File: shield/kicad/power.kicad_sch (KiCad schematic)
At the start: 23 parts, among them Q1 NTR4101PT1G, Q2 DMG1012T-7, Q3 DMG1012T-7, Q4 NTR4101PT1G, Q5 DMG1012T-7, Q6 DMG1012T-7, U1 BQ25060DQCR, U2 Texas Instruments TPS3422EGDR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, U3 STC3100IST, U4 Texas Instruments TPS63060DSCR, U5 MAX803SQ293D2T1G

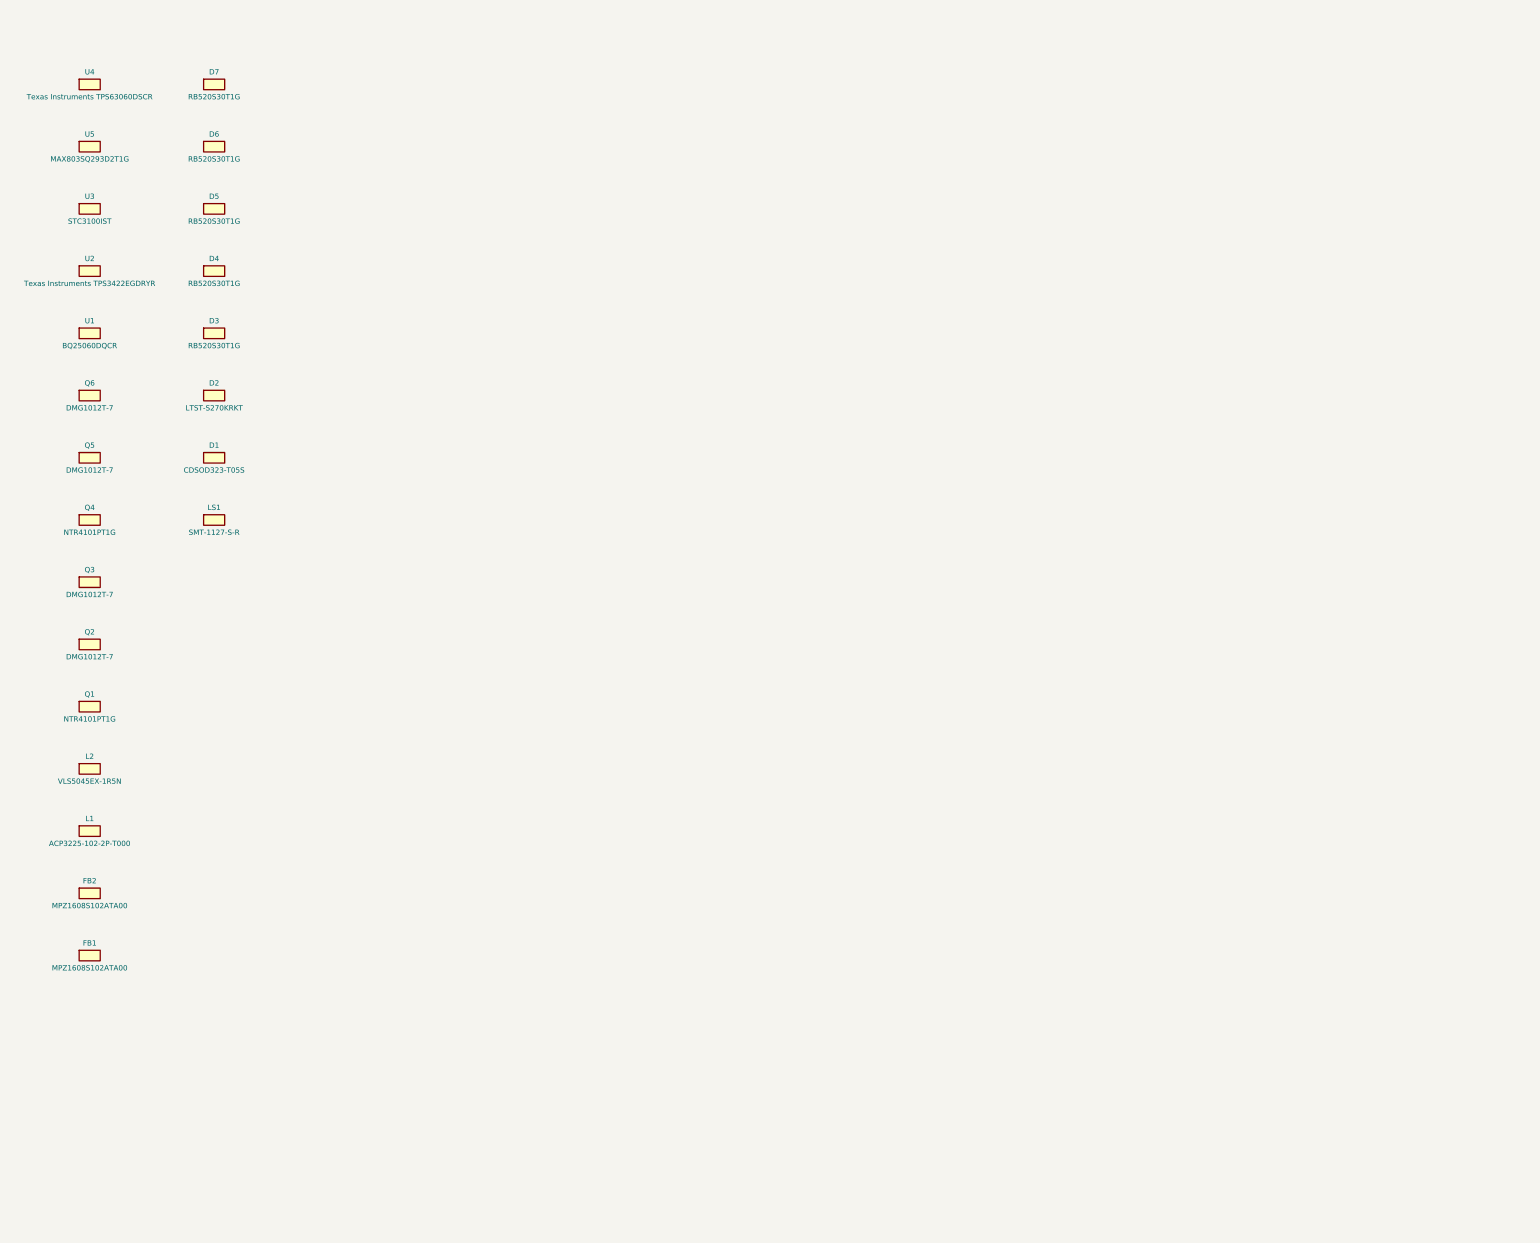
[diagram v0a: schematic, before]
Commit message: Complete schematic wiring, footprint assignments, and validation renders
- Generated proper KiCad symbols with pin definitions for all 139 components
- Created 2 hierarchical sub-sheets: Power Supply and Peripherals & Connectors
- Added schematic wiring with net labels (VBUS, VBAT, V3V3, GND, I2C, SPI, etc.)
- Assigned KiCad standard library footprints to all components
- Rendered schematic and PCB SVGs using kicad-cli-nightly
- Ran ERC and DRC validation
- Updated README with rendered images and footprint assignment table

Agent-Logs-Url: https://github.com/3rdIteration/specter-diy/sessions/67aa0d59-b533-4f87-a3fd-0109cc63ae2b

Co-authored-by: 3rdIteration <2230318+3rdIteration@users.noreply.github.com>
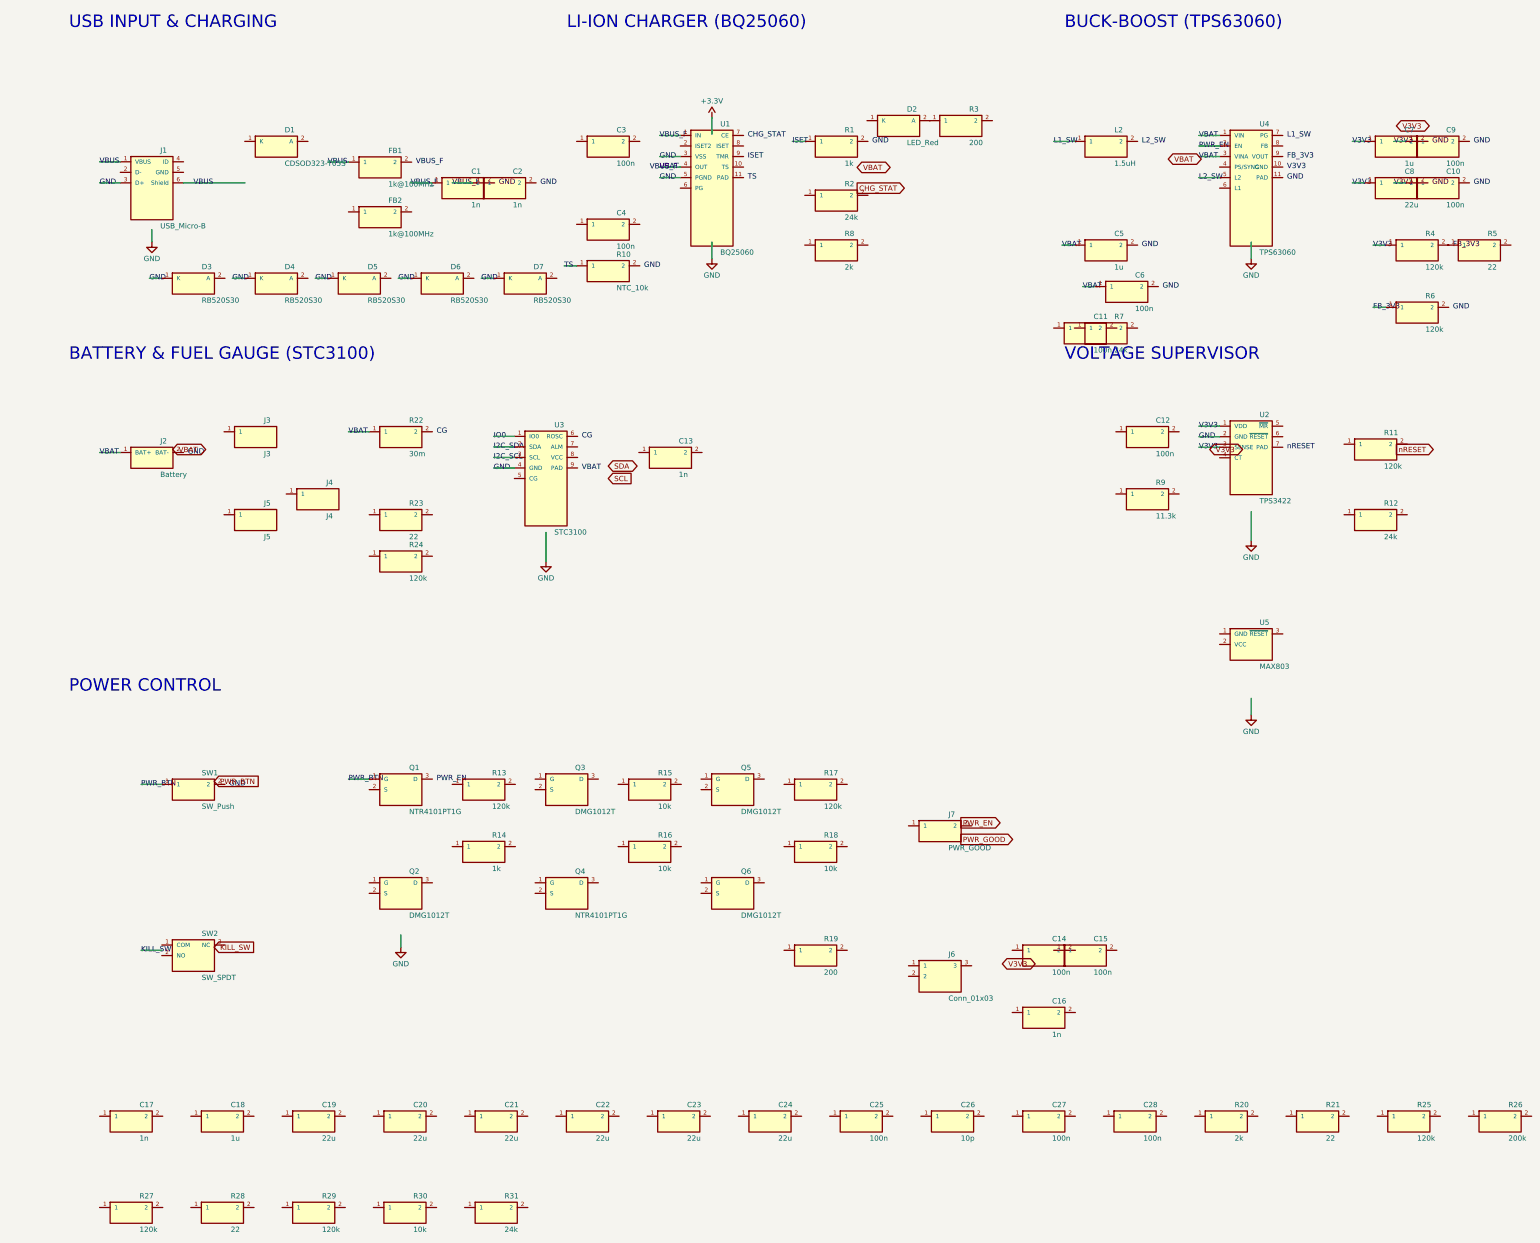
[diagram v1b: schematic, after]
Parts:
- removed D1: CDSOD323-T05S, PCB-svuptgvsz8fymjeirekr-1, symbol specter_shield:D1
- removed D2: LTST-S270KRKT, PCB_-_LS_A67K, symbol specter_shield:D2
- removed D3: RB520S30T1G, ONSC-SOD-523-2-502-01_V, symbol specter_shield:D3
- removed D4: RB520S30T1G, ONSC-SOD-523-2-502-01_V, symbol specter_shield:D4
- removed D5: RB520S30T1G, ONSC-SOD-523-2-502-01_V, symbol specter_shield:D5
- removed D6: RB520S30T1G, ONSC-SOD-523-2-502-01_V, symbol specter_shield:D6
- removed D7: RB520S30T1G, ONSC-SOD-523-2-502-01_V, symbol specter_shield:D7
- removed FB1: MPZ1608S102ATA00, PCB-lzgidm1lbgbngdte6jvy-1, symbol specter_shield:FB1
- removed FB2: MPZ1608S102ATA00, PCB-lzgidm1lbgbngdte6jvy-1, symbol specter_shield:FB2
- removed L1: ACP3225-102-2P-T000, PCB-59e4j6y0bn8hbujw2jpq-1, symbol specter_shield:L1
- removed L2: VLS5045EX-1R5N, VLS5045EX-1R5N, symbol specter_shield:L2
- removed LS1: SMT-1127-S-R, PCB-s69sc097nywe4t4ay05e-1, symbol specter_shield:LS1
- removed Q1: NTR4101PT1G, ONSC-SOT-23-3-318-08_V, symbol specter_shield:Q1
- removed Q2: DMG1012T-7, PCB-829213-1, symbol specter_shield:Q2
- removed Q3: DMG1012T-7, PCB-829213-1, symbol specter_shield:Q3
- removed Q4: NTR4101PT1G, ONSC-SOT-23-3-318-08_V, symbol specter_shield:Q4
- removed Q5: DMG1012T-7, PCB-829213-1, symbol specter_shield:Q5
- removed Q6: DMG1012T-7, PCB-829213-1, symbol specter_shield:Q6
- removed U1: BQ25060DQCR, DQC10-2400X840TP, symbol specter_shield:U1
- removed U2: Texas Instruments TPS3422EGDRYR, PCB-yhvz6iwei78a9n514jnh-1, symbol specter_shield:U2
- removed U3: STC3100IST, PCB-2tv7dotjw6i7jk8dmo5t-1, symbol specter_shield:U3
- removed U4: Texas Instruments TPS63060DSCR, TPS63060, symbol specter_shield:U4
- removed U5: MAX803SQ293D2T1G, PCB-cot7ps8saw6rws0ryicd-1, symbol specter_shield:U5
- added C1: 1n, Capacitor_SMD:C_0402_1005Metric, symbol C1
- added C10: 100n, Capacitor_SMD:C_0402_1005Metric, symbol C10
- added C11: 100n, Capacitor_SMD:C_0402_1005Metric, symbol C11
- added C12: 100n, Capacitor_SMD:C_0402_1005Metric, symbol C12
- added C13: 1n, Capacitor_SMD:C_0402_1005Metric, symbol C13
- added C14: 100n, Capacitor_SMD:C_0402_1005Metric, symbol C14
- added C15: 100n, Capacitor_SMD:C_0402_1005Metric, symbol C15
- added C16: 1n, Capacitor_SMD:C_0402_1005Metric, symbol C16
- added C17: 1n, Capacitor_SMD:C_0402_1005Metric, symbol C17
- added C18: 1u, Capacitor_SMD:C_0402_1005Metric, symbol C18
- added C19: 22u, Capacitor_SMD:C_0805_2012Metric, symbol C19
- added C2: 1n, Capacitor_SMD:C_0402_1005Metric, symbol C2
- added C20: 22u, Capacitor_SMD:C_0805_2012Metric, symbol C20
- added C21: 22u, Capacitor_SMD:C_0805_2012Metric, symbol C21
- added C22: 22u, Capacitor_SMD:C_0805_2012Metric, symbol C22
- added C23: 22u, Capacitor_SMD:C_0805_2012Metric, symbol C23
- added C24: 22u, Capacitor_SMD:C_0805_2012Metric, symbol C24
- added C25: 100n, Capacitor_SMD:C_0402_1005Metric, symbol C25
- added C26: 10p, Capacitor_SMD:C_0402_1005Metric, symbol C26
- added C27: 100n, Capacitor_SMD:C_0402_1005Metric, symbol C27
- added C28: 100n, Capacitor_SMD:C_0402_1005Metric, symbol C28
- added C3: 100n, Capacitor_SMD:C_0402_1005Metric, symbol C3
- added C4: 100n, Capacitor_SMD:C_0402_1005Metric, symbol C4
- added C5: 1u, Capacitor_SMD:C_0402_1005Metric, symbol C5
- added C6: 100n, Capacitor_SMD:C_0402_1005Metric, symbol C6
- added C7: 1u, Capacitor_SMD:C_0402_1005Metric, symbol C7
- added C8: 22u, Capacitor_SMD:C_0805_2012Metric, symbol C8
- added C9: 100n, Capacitor_SMD:C_0402_1005Metric, symbol C9
- added D1: CDSOD323-T05S, Diode_SMD:D_SOD-323, symbol D1
- added D2: LED_Red, LED_SMD:LED_0603_1608Metric, symbol D2
- added D3: RB520S30, Diode_SMD:D_SOD-523, symbol D3
- added D4: RB520S30, Diode_SMD:D_SOD-523, symbol D4
- added D5: RB520S30, Diode_SMD:D_SOD-523, symbol D5
- added D6: RB520S30, Diode_SMD:D_SOD-523, symbol D6
- added D7: RB520S30, Diode_SMD:D_SOD-523, symbol D7
- added FB1: 1k@100MHz, Inductor_SMD:L_0603_1608Metric, symbol FB1
- added FB2: 1k@100MHz, Inductor_SMD:L_0603_1608Metric, symbol FB2
- added J1: USB_Micro-B, Connector_USB:USB_Micro-B_Molex_47346-0001, symbol J1
- added J2: Battery, Connector_JST:JST_PH_S2B-PH-SM4-TB_1x02-1MP_P2.00mm_Horizontal, symbol J2
- added J3: J3, TestPoint:TestPoint_Pad_D1.0mm, symbol J3
- added J4: J4, TestPoint:TestPoint_Pad_D1.0mm, symbol J4
- added J5: J5, TestPoint:TestPoint_Pad_D1.0mm, symbol J5
- added J6: Conn_01x03, Connector_JST:JST_PH_S3B-PH-SM4-TB_1x03-1MP_P2.00mm_Horizontal, symbol J6
- added J7: PWR_GOOD, Connector_PinHeader_2.54mm:PinHeader_1x02_P2.54mm_Vertical, symbol J7
- added L2: 1.5uH, Inductor_SMD:L_Taiyo-Yuden_NR-50xx_HandSoldering, symbol L2
- added Q1: NTR4101PT1G, Package_TO_SOT_SMD:SOT-23, symbol Q1
- added Q2: DMG1012T, Package_TO_SOT_SMD:SOT-523, symbol Q2
- added Q3: DMG1012T, Package_TO_SOT_SMD:SOT-523, symbol Q3
- added Q4: NTR4101PT1G, Package_TO_SOT_SMD:SOT-23, symbol Q4
- added Q5: DMG1012T, Package_TO_SOT_SMD:SOT-523, symbol Q5
- added Q6: DMG1012T, Package_TO_SOT_SMD:SOT-523, symbol Q6
- added R1: 1k, Resistor_SMD:R_0402_1005Metric, symbol R1
- added R10: NTC_10k, Resistor_SMD:R_0402_1005Metric, symbol R10
- added R11: 120k, Resistor_SMD:R_0402_1005Metric, symbol R11
- added R12: 24k, Resistor_SMD:R_0402_1005Metric, symbol R12
- added R13: 120k, Resistor_SMD:R_0402_1005Metric, symbol R13
- added R14: 1k, Resistor_SMD:R_0402_1005Metric, symbol R14
- added R15: 10k, Resistor_SMD:R_0402_1005Metric, symbol R15
- added R16: 10k, Resistor_SMD:R_0402_1005Metric, symbol R16
- added R17: 120k, Resistor_SMD:R_0402_1005Metric, symbol R17
- added R18: 10k, Resistor_SMD:R_0402_1005Metric, symbol R18
- added R19: 200, Resistor_SMD:R_0402_1005Metric, symbol R19
- added R2: 24k, Resistor_SMD:R_0402_1005Metric, symbol R2
- added R20: 2k, Resistor_SMD:R_0402_1005Metric, symbol R20
- added R21: 22, Resistor_SMD:R_0402_1005Metric, symbol R21
- added R22: 30m, Resistor_SMD:R_0805_2012Metric, symbol R22
- added R23: 22, Resistor_SMD:R_0402_1005Metric, symbol R23
- added R24: 120k, Resistor_SMD:R_0402_1005Metric, symbol R24
- added R25: 120k, Resistor_SMD:R_0402_1005Metric, symbol R25
- added R26: 200k, Resistor_SMD:R_0402_1005Metric, symbol R26
- added R27: 120k, Resistor_SMD:R_0402_1005Metric, symbol R27
- added R28: 22, Resistor_SMD:R_0402_1005Metric, symbol R28
- added R29: 120k, Resistor_SMD:R_0402_1005Metric, symbol R29
- added R3: 200, Resistor_SMD:R_0402_1005Metric, symbol R3
- added R30: 10k, Resistor_SMD:R_0402_1005Metric, symbol R30
- added R31: 24k, Resistor_SMD:R_0402_1005Metric, symbol R31
- added R4: 120k, Resistor_SMD:R_0402_1005Metric, symbol R4
- added R5: 22, Resistor_SMD:R_0402_1005Metric, symbol R5
- added R6: 120k, Resistor_SMD:R_0402_1005Metric, symbol R6
- added R7: 24k, Resistor_SMD:R_0402_1005Metric, symbol R7
- added R8: 2k, Resistor_SMD:R_0402_1005Metric, symbol R8
- added R9: 11.3k, Resistor_SMD:R_0402_1005Metric, symbol R9
- added SW1: SW_Push, Button_Switch_SMD:SW_SPST_CK_RS282G05A3, symbol SW1
- added SW2: SW_SPDT, Button_Switch_SMD:SW_SPDT_CK_OS102011MA1QN1, symbol SW2
- added U1: BQ25060, Package_DFN_QFN:DFN-10-1EP_2.5x2.5mm_P0.5mm_EP1.0x1.5mm, symbol U1
- added U2: TPS3422, Package_DFN_QFN:DFN-6-1EP_2x2mm_P0.65mm_EP0.64x1.015mm, symbol U2
- added U3: STC3100, Package_DFN_QFN:DFN-8-1EP_3x3mm_P0.5mm_EP1.75x2.35mm, symbol U3
- added U4: TPS63060, Package_SON:VSON-10-1EP_3x3mm_P0.5mm_EP1.2x2mm, symbol U4
- added U5: MAX803, Package_TO_SOT_SMD:SOT-23, symbol U5
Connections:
- new net FB_3V3: R6.1
- new net GND: D3.1 (K), D4.1 (K), D5.1 (K), D6.1 (K), D7.1 (K), J1.3 (D+), U1.3 (VSS), U1.5 (PGND), U2.2 (GND), U3.4 (GND)
- new net I2C_SCL: U3.3 (SCL)
- new net I2C_SDA: U3.2 (SDA)
- new net IO0: U3.1 (IO0)
- new net ISET: R1.1
- new net L1_SW: L2.1
- new net L2_SW: U4.5 (L2)
- new net PWR_BTN: Q1.1 (G), SW1.1
- new net PWR_EN: U4.2 (EN)
- new net TS: R10.1
- new net V3V3: C10.1, C7.1, C8.1, C9.1, R4.1, U2.1 (VDD), U2.3 (SENSE)
- new net VBAT: C5.1, C6.1, J2.1 (BAT+), R22.1, U1.4 (OUT), U4.1 (VIN), U4.3 (VINA)
- new net VBUS: FB1.1, J1.1 (VBUS), J1.6 (Shield)
- new net VBUS_F: C1.1, C2.1, U1.1 (IN)
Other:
- note added: "BATTERY & FUEL GAUGE (STC3100)"
- note added: "BUCK-BOOST (TPS63060)"
- note added: "LI-ION CHARGER (BQ25060)"
- note added: "POWER CONTROL"
- note added: "USB INPUT & CHARGING"
- note added: "VOLTAGE SUPERVISOR"
- title: Specter Shield v1 - Power -> Specter Shield v1 - Power Supply
